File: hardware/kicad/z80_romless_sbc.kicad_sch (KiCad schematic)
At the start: 40 parts, among them J1 REGULATED 5V INPUT, J2 PICO GPIO EXPANSION, U1 Z84C0020PEC, U10 SN74LVC245AN bus-to-Pico, U2 AS6C1008-55PCN, U3 SN74HCT32N, U4 SN74AHCT244N, U7 SN74LVC244AN, U9 SN74AHCT245N Pico-to-bus

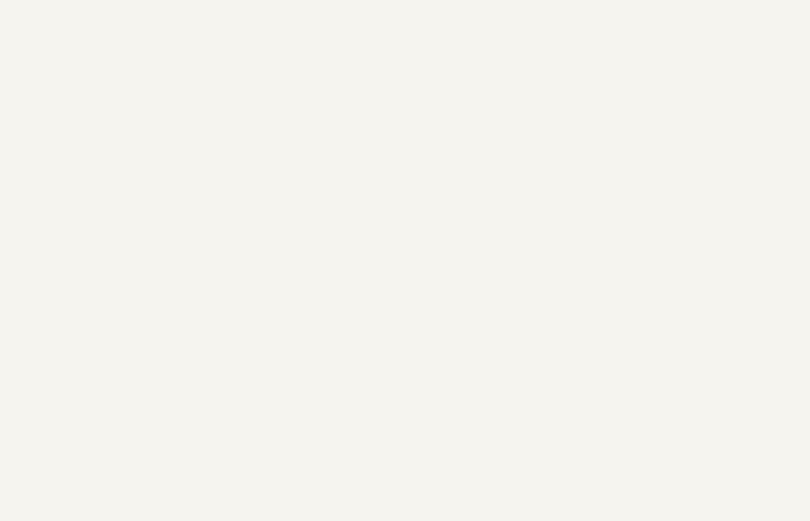
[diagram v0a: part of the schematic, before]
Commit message: Add native CP/M auto-run and Pico VSYS hold-up capacitor
Implement board-native auto-run configuration and boot handling, and add
local VSYS capacitance to improve USB-disconnect behaviour.

Native CP/M auto-run
- Add AUTORUN.COM with cold-only, warm-only, both, and disabled modes.
- Accept printable commands up to 80 characters, normalize them to
  uppercase, and allow existing settings to be retained or changes
  cancelled without writing.
- Store configuration in drive A's final reserved system record:
  LBA 63, track 1 sector 31, image offset 0x1F80.
- Define a versioned ZAR1 record with mode, command length, command text,
  and an additive checksum.
- Require the native BIOS signature, use a directory-type write for
  journaled durability, and verify the entire record by read-back.
- Preserve the caller's default drive and report read, write, and
  verification failures explicitly.

BIOS and image generation
- Validate and apply auto-run settings on cold and warm boot, reporting
  invalid configuration without executing it.
- Allow a pending console key to bypass an applicable auto-run command,
  while leaving input untouched for disabled or inapplicable modes.
- Clear the CCP command length on each boot and enter through its cold
  vector so cold-only commands do not repeat after transient warm boots.
- Move the BIOS directory buffer into reserved BDOS padding at
  FC80h-FCFFh without reducing the TPA, and guard against image overlap.
- Assemble and export AUTORUN.COM, replace the Altair utility on generated
  drive A, and initialize new auto-run settings to disabled.
- Add CMake dependencies, artifact metadata, cpmtools requirements, and
  provisioning guidance for matching boot packages and native drive A.

Regression coverage
- Add image-format, checksum, command-boundary, workspace-overlap, and
  utility-installation tests, including preservation of other files.
- Extend real Z80 execution tests for boot modes, repeated warm boots,
  keyboard bypass, utili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
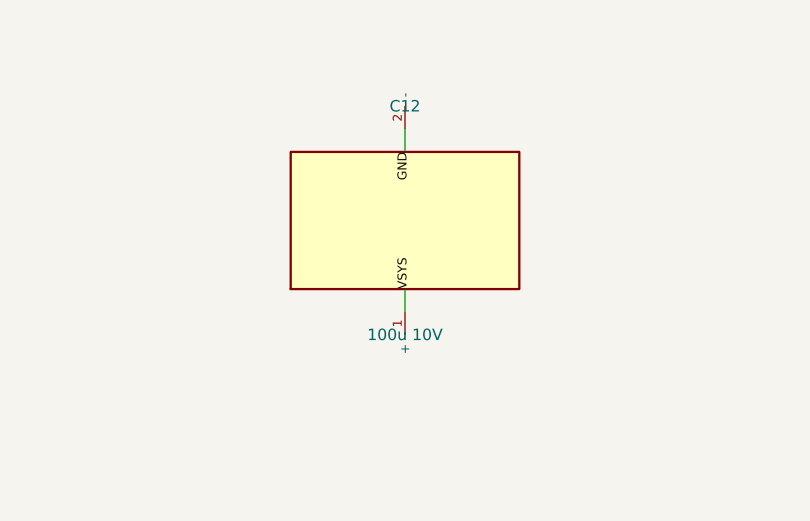
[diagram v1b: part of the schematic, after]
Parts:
- added C12: 100u 10V, Capacitor_THT:CP_Radial_D10.0mm_P5.00mm, symbol Z80SBC:CAPACITOR
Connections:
- net GND: now also C12.2 (-)
- net VSYS: now also C12.1 (+)
